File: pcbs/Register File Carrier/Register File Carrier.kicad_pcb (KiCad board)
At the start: 2 copper layers, 15 parts, among them J1001 Conn_02x20_Odd_Even, J1002 Conn_02x20_Odd_Even, U2001 74AHC04, U3001 74HC14, U3002 74HC08, U3003 74HC138, U3004 74HC08, U4001 74HC245, U4002 74HC245, U5001 74HC245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

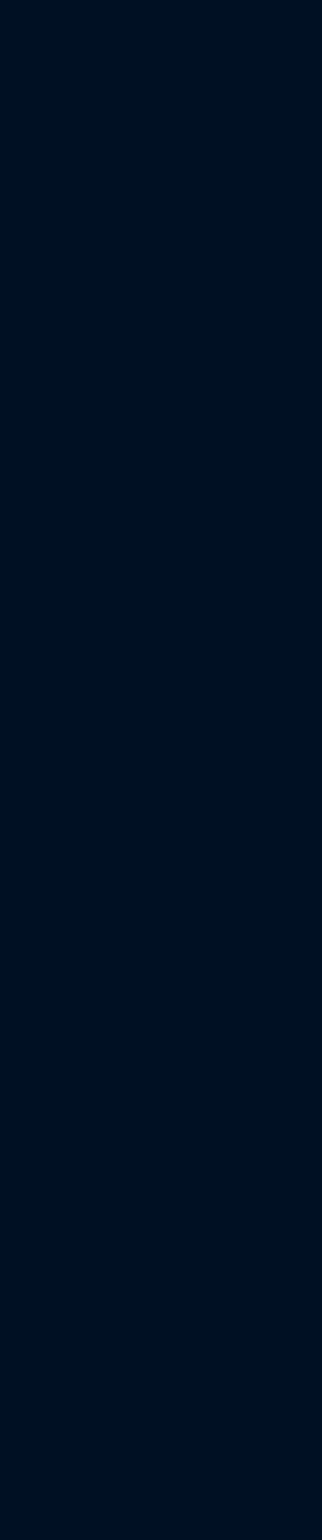
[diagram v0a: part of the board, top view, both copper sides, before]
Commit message: Setting up some LEDs
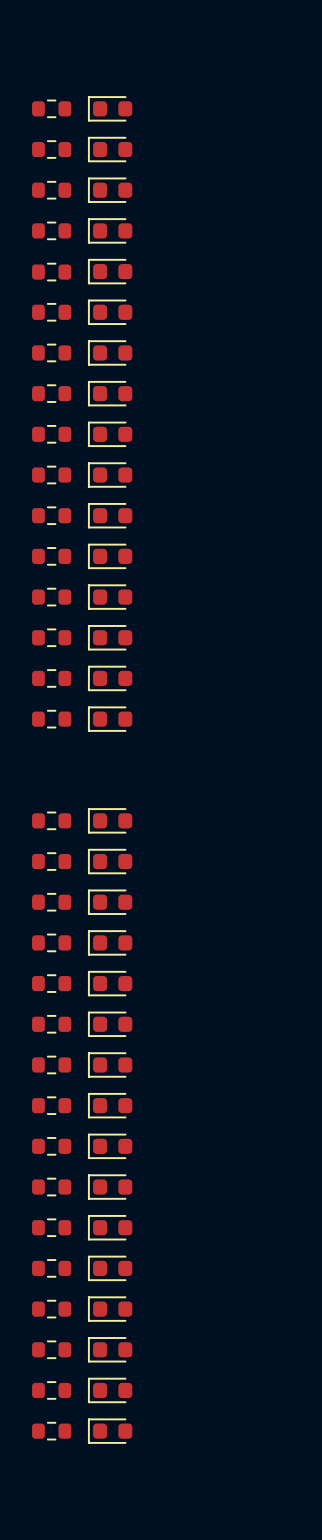
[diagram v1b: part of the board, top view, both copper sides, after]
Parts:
- added D4001: WHITE, LED_SMD:LED_0603_1608Metric, F.Cu at (71.8, 118.7)
- added D4002: WHITE, LED_SMD:LED_0603_1608Metric, F.Cu at (71.8, 121.3)
- added D4003: WHITE, LED_SMD:LED_0603_1608Metric, F.Cu at (71.8, 123.8)
- added D4004: WHITE, LED_SMD:LED_0603_1608Metric, F.Cu at (71.8, 126.4)
- added D4005: WHITE, LED_SMD:LED_0603_1608Metric, F.Cu at (71.8, 128.9)
- added D4006: WHITE, LED_SMD:LED_0603_1608Metric, F.Cu at (71.8, 131.4)
- added D4007: WHITE, LED_SMD:LED_0603_1608Metric, F.Cu at (71.8, 134.0)
- added D4008: WHITE, LED_SMD:LED_0603_1608Metric, F.Cu at (71.8, 136.5)
- added D4009: WHITE, LED_SMD:LED_0603_1608Metric, F.Cu at (71.8, 139.1)
- added D4010: WHITE, LED_SMD:LED_0603_1608Metric, F.Cu at (71.8, 141.6)
- added D4011: WHITE, LED_SMD:LED_0603_1608Metric, F.Cu at (71.8, 144.1)
- added D4012: WHITE, LED_SMD:LED_0603_1608Metric, F.Cu at (71.8, 146.7)
- added D4013: WHITE, LED_SMD:LED_0603_1608Metric, F.Cu at (71.8, 149.2)
- added D4014: WHITE, LED_SMD:LED_0603_1608Metric, F.Cu at (71.8, 151.8)
- added D4015: WHITE, LED_SMD:LED_0603_1608Metric, F.Cu at (71.8, 154.3)
- added D4016: WHITE, LED_SMD:LED_0603_1608Metric, F.Cu at (71.8, 156.8)
- added D5001: WHITE, LED_SMD:LED_0603_1608Metric, F.Cu at (71.8, 163.2)
- added D5002: WHITE, LED_SMD:LED_0603_1608Metric, F.Cu at (71.8, 165.7)
- added D5003: WHITE, LED_SMD:LED_0603_1608Metric, F.Cu at (71.8, 168.3)
- added D5004: WHITE, LED_SMD:LED_0603_1608Metric, F.Cu at (71.8, 170.8)
- added D5005: WHITE, LED_SMD:LED_0603_1608Metric, F.Cu at (71.8, 173.4)
- added D5006: WHITE, LED_SMD:LED_0603_1608Metric, F.Cu at (71.8, 175.9)
- added D5007: WHITE, LED_SMD:LED_0603_1608Metric, F.Cu at (71.8, 178.4)
- added D5008: WHITE, LED_SMD:LED_0603_1608Metric, F.Cu at (71.8, 181.0)
- added D5009: WHITE, LED_SMD:LED_0603_1608Metric, F.Cu at (71.8, 183.5)
- added D5010: WHITE, LED_SMD:LED_0603_1608Metric, F.Cu at (71.8, 186.1)
- added D5011: WHITE, LED_SMD:LED_0603_1608Metric, F.Cu at (71.8, 188.6)
- added D5012: WHITE, LED_SMD:LED_0603_1608Metric, F.Cu at (71.8, 191.1)
- added D5013: WHITE, LED_SMD:LED_0603_1608Metric, F.Cu at (71.8, 193.7)
- added D5014: WHITE, LED_SMD:LED_0603_1608Metric, F.Cu at (71.8, 196.2)
- added D5015: WHITE, LED_SMD:LED_0603_1608Metric, F.Cu at (71.8, 198.8)
- added D5016: WHITE, LED_SMD:LED_0603_1608Metric, F.Cu at (71.8, 201.3)
- added R4001: 4k7, Resistor_SMD:R_0603_1608Metric, F.Cu at (67.9, 118.7)
- added R4002: 4k7, Resistor_SMD:R_0603_1608Metric, F.Cu at (67.9, 121.3)
- added R4003: 4k7, Resistor_SMD:R_0603_1608Metric, F.Cu at (67.9, 123.8)
- added R4004: 4k7, Resistor_SMD:R_0603_1608Metric, F.Cu at (67.9, 126.4)
- added R4005: 4k7, Resistor_SMD:R_0603_1608Metric, F.Cu at (67.9, 128.9)
- added R4006: 4k7, Resistor_SMD:R_0603_1608Metric, F.Cu at (67.9, 131.4)
- added R4007: 4k7, Resistor_SMD:R_0603_1608Metric, F.Cu at (67.9, 134.0)
- added R4008: 4k7, Resistor_SMD:R_0603_1608Metric, F.Cu at (67.9, 136.5)
- added R4009: 4k7, Resistor_SMD:R_0603_1608Metric, F.Cu at (67.9, 139.1)
- added R4010: 4k7, Resistor_SMD:R_0603_1608Metric, F.Cu at (67.9, 141.6)
- added R4011: 4k7, Resistor_SMD:R_0603_1608Metric, F.Cu at (67.9, 144.1)
- added R4012: 4k7, Resistor_SMD:R_0603_1608Metric, F.Cu at (67.9, 146.7)
- added R4013: 4k7, Resistor_SMD:R_0603_1608Metric, F.Cu at (67.9, 149.2)
- added R4014: 4k7, Resistor_SMD:R_0603_1608Metric, F.Cu at (67.9, 151.8)
- added R4015: 4k7, Resistor_SMD:R_0603_1608Metric, F.Cu at (67.9, 154.3)
- added R4016: 4k7, Resistor_SMD:R_0603_1608Metric, F.Cu at (67.9, 156.8)
- added R5001: 4k7, Resistor_SMD:R_0603_1608Metric, F.Cu at (67.9, 163.2)
- added R5002: 4k7, Resistor_SMD:R_0603_1608Metric, F.Cu at (67.9, 165.7)
- added R5003: 4k7, Resistor_SMD:R_0603_1608Metric, F.Cu at (67.9, 168.3)
- added R5004: 4k7, Resistor_SMD:R_0603_1608Metric, F.Cu at (67.9, 170.8)
- added R5005: 4k7, Resistor_SMD:R_0603_1608Metric, F.Cu at (67.9, 173.4)
- added R5006: 4k7, Resistor_SMD:R_0603_1608Metric, F.Cu at (67.9, 175.9)
- added R5007: 4k7, Resistor_SMD:R_0603_1608Metric, F.Cu at (67.9, 178.4)
- added R5008: 4k7, Resistor_SMD:R_0603_1608Metric, F.Cu at (67.9, 181.0)
- added R5009: 4k7, Resistor_SMD:R_0603_1608Metric, F.Cu at (67.9, 183.5)
- added R5010: 4k7, Resistor_SMD:R_0603_1608Metric, F.Cu at (67.9, 186.1)
- added R5011: 4k7, Resistor_SMD:R_0603_1608Metric, F.Cu at (67.9, 188.6)
- added R5012: 4k7, Resistor_SMD:R_0603_1608Metric, F.Cu at (67.9, 191.1)
- added R5013: 4k7, Resistor_SMD:R_0603_1608Metric, F.Cu at (67.9, 193.7)
- added R5014: 4k7, Resistor_SMD:R_0603_1608Metric, F.Cu at (67.9, 196.2)
- added R5015: 4k7, Resistor_SMD:R_0603_1608Metric, F.Cu at (67.9, 198.8)
- added R5016: 4k7, Resistor_SMD:R_0603_1608Metric, F.Cu at (67.9, 201.3)
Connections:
- net /Connector Block/C0 renamed /C0
- net /Connector Block/C1 renamed /C1
- net /Connector Block/C10 renamed /C10
- net /Connector Block/C11 renamed /C11
- net /Connector Block/C12 renamed /C12
- net /Connector Block/C13 renamed /C13
- net /Connector Block/C14 renamed /C14
- net /Connector Block/C15 renamed /C15
- net /Connector Block/C2 renamed /C2
- net /Connector Block/C3 renamed /C3
- net /Connector Block/C4 renamed /C4
- net /Connector Block/C5 renamed /C5
- net /Connector Block/C6 renamed /C6
- net /Connector Block/C7 renamed /C7
- net /Connector Block/C8 renamed /C8
- net /Connector Block/C9 renamed /C9
- net /Enabler/Cycle2 renamed /Cycle2
- net /Enabler/Cycle3 renamed /Cycle3
- net /Enabler/Cycle4 renamed /Cycle4
- net /Enabler/I0 renamed /I0
- net /Enabler/I1 renamed /I1
- net /Enabler/I2 renamed /I2
- net /Enabler/I3 renamed /I3
- U3004 pad 14: unconnected-(U3004E-VCC-Pad14) -> +5V
- U3004 pad 7: unconnected-(U3004E-GND-Pad7) -> GND

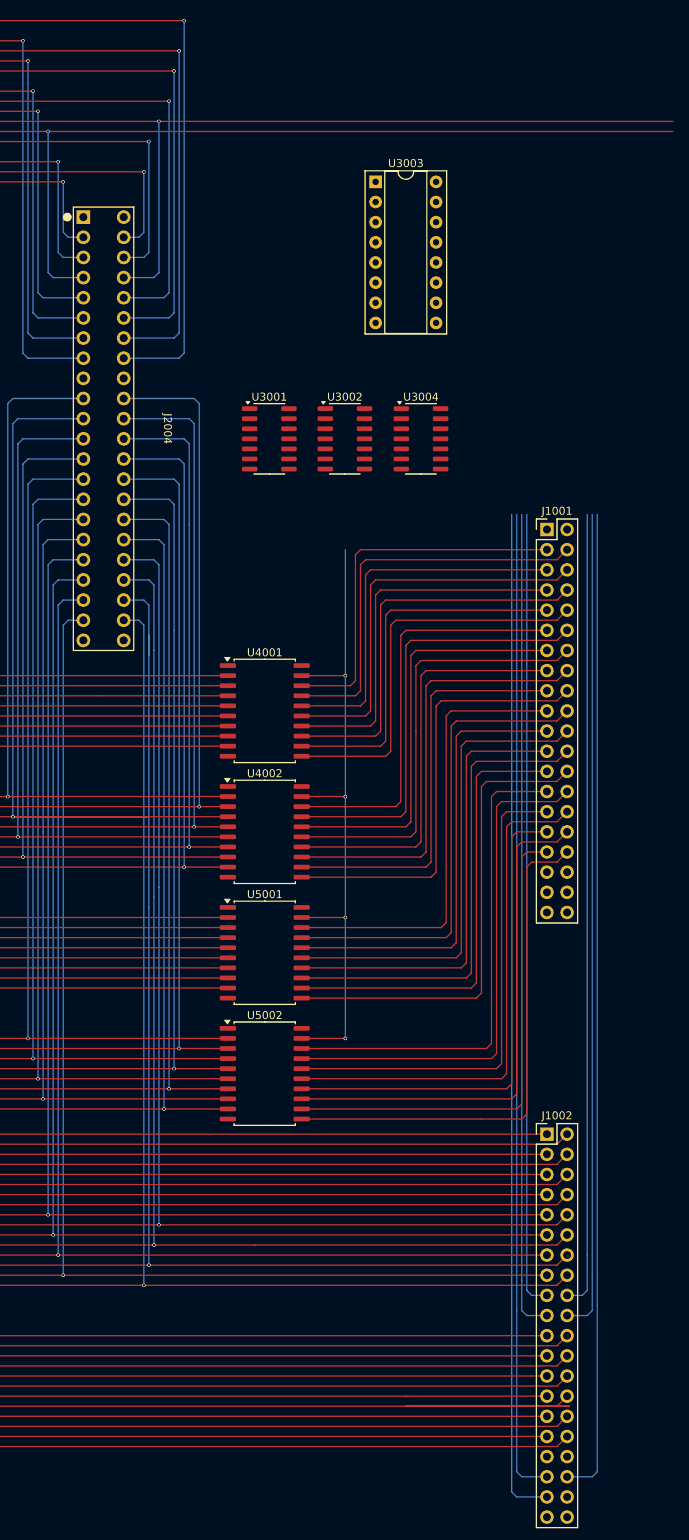
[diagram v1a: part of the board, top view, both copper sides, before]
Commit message: More LEDs and routing
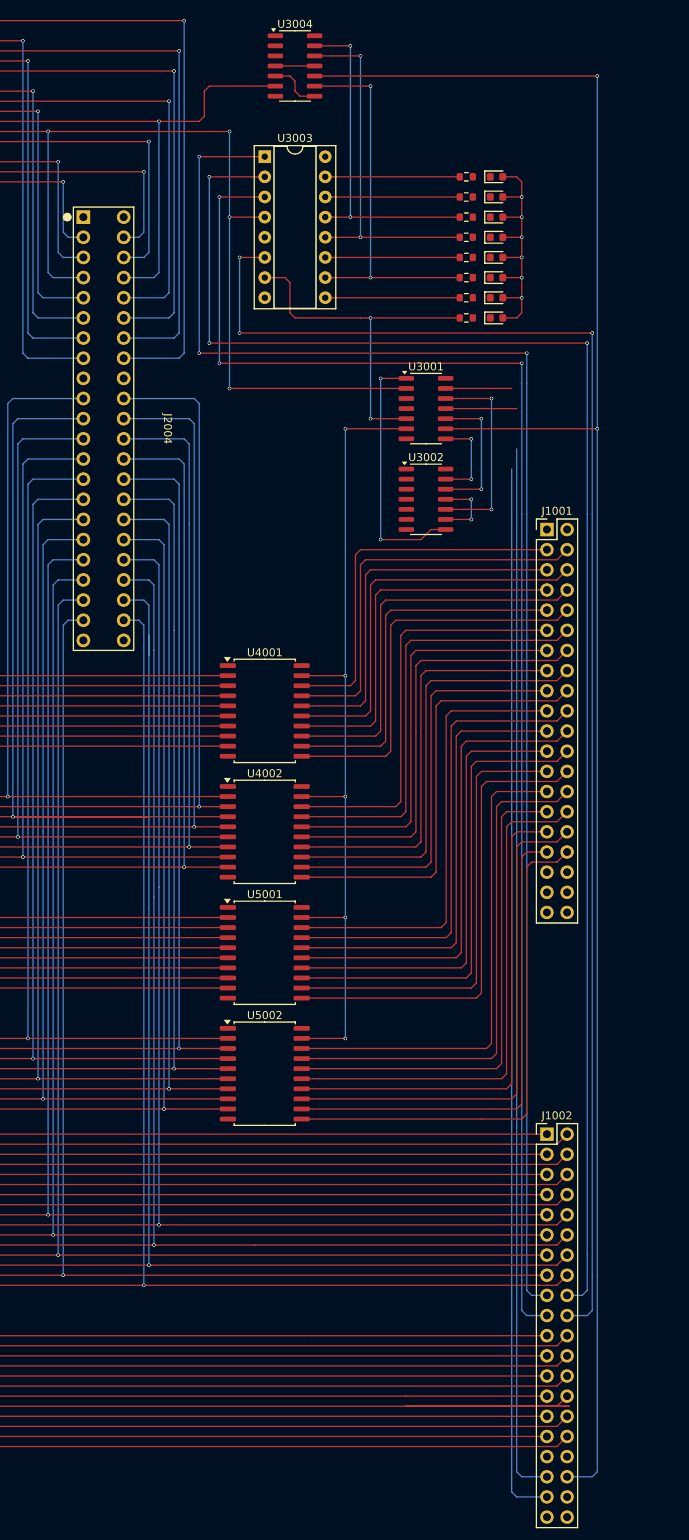
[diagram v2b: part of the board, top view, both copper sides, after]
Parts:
- added D3001: Blue, LED_SMD:LED_0603_1608Metric, F.Cu at (278.1, 69.8)
- added D3002: Blue, LED_SMD:LED_0603_1608Metric, F.Cu at (278.1, 72.4)
- added D3003: Blue, LED_SMD:LED_0603_1608Metric, F.Cu at (278.1, 74.9)
- added D3004: Blue, LED_SMD:LED_0603_1608Metric, F.Cu at (278.1, 77.5)
- added D3005: Blue, LED_SMD:LED_0603_1608Metric, F.Cu at (278.1, 80.0)
- added D3006: Blue, LED_SMD:LED_0603_1608Metric, F.Cu at (278.1, 82.5)
- added D3007: Blue, LED_SMD:LED_0603_1608Metric, F.Cu at (278.1, 85.1)
- added D3008: Blue, LED_SMD:LED_0603_1608Metric, F.Cu at (278.1, 87.6)
- added R3001: 4k7, Resistor_SMD:R_0603_1608Metric, F.Cu at (274.3, 69.8)
- added R3002: 4k7, Resistor_SMD:R_0603_1608Metric, F.Cu at (274.3, 72.4)
- added R3003: 4k7, Resistor_SMD:R_0603_1608Metric, F.Cu at (274.3, 74.9)
- added R3004: 4k7, Resistor_SMD:R_0603_1608Metric, F.Cu at (274.3, 77.5)
- added R3005: 4k7, Resistor_SMD:R_0603_1608Metric, F.Cu at (274.3, 80.0)
- added R3006: 4k7, Resistor_SMD:R_0603_1608Metric, F.Cu at (274.3, 82.5)
- added R3007: 4k7, Resistor_SMD:R_0603_1608Metric, F.Cu at (274.3, 85.1)
- added R3008: 4k7, Resistor_SMD:R_0603_1608Metric, F.Cu at (274.3, 87.6)
- moved U3004 49.6 mm to (252.7, 55.9)
- moved U3001 20.1 mm to (269.2, 99.1)
- moved U3003 14.3 mm to (248.9, 67.3)
- moved U3002 12.8 mm to (269.2, 110.5)
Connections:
- U3001 pad 11: /Cycle3 -> /Cycle2
- U3001 pad 13: /Cycle2 -> /Cycle4
- U3001 pad 3: /Enabler/~{Set} -> GND
- U3001 pad 4: /Enabler/~{AB_{Enable}} -> unconnected-(U3001-Pad4)
- U3001 pad 5: /Cycle4 -> /Enabler/~{Set}
- U3001 pad 6: Net-(U3001-Pad6) -> /Enabler/~{AB_{Enable}}
- U3001 pad 8: unconnected-(U3001-Pad8) -> Net-(U3001-Pad8)
- U3001 pad 9: GND -> /Cycle3
- U3002 pad 1: Net-(U3001-Pad12) -> GND
- U3002 pad 10: GND -> Net-(U3001-Pad12)
- U3002 pad 11: unconnected-(U3002-Pad11) -> Net-(U3002-Pad11)
- U3002 pad 12: GND -> Net-(U3001-Pad10)
- U3002 pad 13: GND -> Net-(U3001-Pad8)
- U3002 pad 2: Net-(U3001-Pad10) -> GND
- U3002 pad 3: Net-(U3002-Pad3) -> unconnected-(U3002-Pad3)
- U3002 pad 4: Net-(U3002-Pad3) -> GND
- U3002 pad 5: Net-(U3001-Pad6) -> GND
- U3002 pad 6: Net-(U3001-Pad1) -> unconnected-(U3002-Pad6)
- U3002 pad 8: unconnected-(U3002-Pad8) -> Net-(U3001-Pad1)
- U3002 pad 9: GND -> Net-(U3002-Pad11)
- U3004 pad 4: Net-(U3004-Pad4) -> Net-(U3004-Pad11)
- U3004 pad 5: Net-(U3004-Pad11) -> Net-(U3004-Pad5)
- U3004 pad 8: Net-(U3004-Pad4) -> Net-(U3004-Pad5)
- U4001 pad 1: unconnected-(U4001-A->B-Pad1) -> +5V
- U4002 pad 1: unconnected-(U4002-A->B-Pad1) -> +5V
- U5001 pad 1: unconnected-(U5001-A->B-Pad1) -> +5V
- U5002 pad 1: unconnected-(U5002-A->B-Pad1) -> +5V
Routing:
- net /Cycle3: track 124.7 -> 234.7 mm, vias 0 -> 2
- net /I1: track 100.6 -> 197.7 mm, vias 0 -> 3
- net /I0: track 100.6 -> 195.2 mm, vias 0 -> 3
- net /I2: track 103.8 -> 187.6 mm, vias 0 -> 3
- net /I3: track 103.8 -> 183.8 mm, vias 0 -> 3
- net /Enabler/~{BranchZero}: track 0.00 -> 48.1 mm, vias 0 -> 2
- net /Connector Block/CLK: track 286.8 -> 240.4 mm
- net /Enabler/~{Set}: track 0.00 -> 46.1 mm, vias 0 -> 2
- net /Enabler/~{StoreW}: track 0.00 -> 45.6 mm, vias 0 -> 2
- net /Enabler/~{StoreB}: track 0.00 -> 43.1 mm, vias 0 -> 2
- net +5V: track 0.00 -> 36.1 mm, vias 0 -> 6
- net Net-(U3001-Pad1): track 0.00 -> 32.3 mm, vias 0 -> 2
- net Net-(U3001-Pad12): track 0.00 -> 25.5 mm, vias 0 -> 2
- net /Enabler/~{AB_{Enable}}: track 83.6 -> 106.6 mm, vias 4 -> 5
- net Net-(U3001-Pad10): track 0.00 -> 17.9 mm, vias 0 -> 2
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
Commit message: Draft of final routing
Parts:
- moved D4001 2.54 mm to (69.2, 118.7)
- moved D4002 2.54 mm to (69.2, 121.3)
- moved D4003 2.54 mm to (69.2, 123.8)
- moved D4004 2.54 mm to (69.2, 126.4)
- moved D4005 2.54 mm to (69.2, 128.9)
- moved D4006 2.54 mm to (69.2, 131.4)
- moved D4007 2.54 mm to (69.2, 134.0)
- moved D4008 2.54 mm to (69.2, 136.5)
- moved D4009 2.54 mm to (69.2, 139.1)
- moved D4010 2.54 mm to (69.2, 141.6)
- moved D4011 2.54 mm to (69.2, 144.1)
- moved D4012 2.54 mm to (69.2, 146.7)
- moved D4013 2.54 mm to (69.2, 149.2)
- moved D4014 2.54 mm to (69.2, 151.8)
- moved D4015 2.54 mm to (69.2, 154.3)
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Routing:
- net /Connector Block/B15: track 249.9 -> 340.4 mm
- net /Connector Block/B13: track 250.5 -> 339.1 mm
- net /Connector Block/A9: track 213.7 -> 302.3 mm
- net /Connector Block/B11: track 251.1 -> 337.9 mm
- net /Connector Block/A11: track 213.0 -> 298.5 mm
- net /Connector Block/B9: track 251.8 -> 336.6 mm
- net /Connector Block/A13: track 212.4 -> 294.7 mm
- net /Connector Block/A15: track 211.8 -> 291.6 mm
- net /Connector Block/B14: track 262.6 -> 336.6 mm
- net /Connector Block/B12: track 264.5 -> 335.3 mm
- net /Connector Block/B10: track 266.4 -> 334.1 mm
- net /Connector Block/A8: track 235.3 -> 301.0 mm
- net /Connector Block/B8: track 268.3 -> 332.8 mm
- net /Connector Block/A10: track 267.7 -> 331.5 mm
- net /Connector Block/A12: track 231.5 -> 293.4 mm
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- added copper zone on B.Cu, net +5V
- added copper zone on F.Cu, net GND
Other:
- board outline added: 238.8 x 213.4 mm
